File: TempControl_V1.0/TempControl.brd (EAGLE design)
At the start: 48.3 x 71.1 mm, 21 parts, among them J1 POWER_JACKPTH_BREAD, J3 10118194-0001LF, J4 6_PIN_SERIAL_CABLEPTH, U1 328P, Y1 16MHz

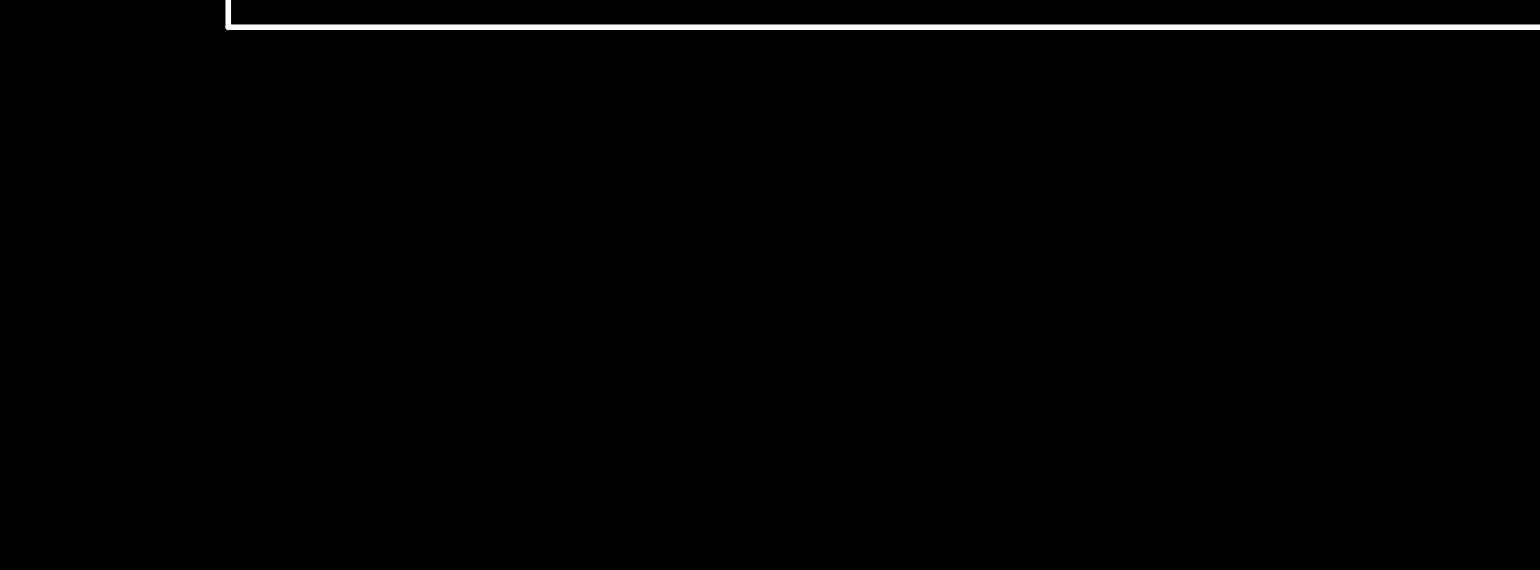
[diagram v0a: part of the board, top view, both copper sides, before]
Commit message: - Added .lbr file for TempControl project - Added OLED part - Rename the project name
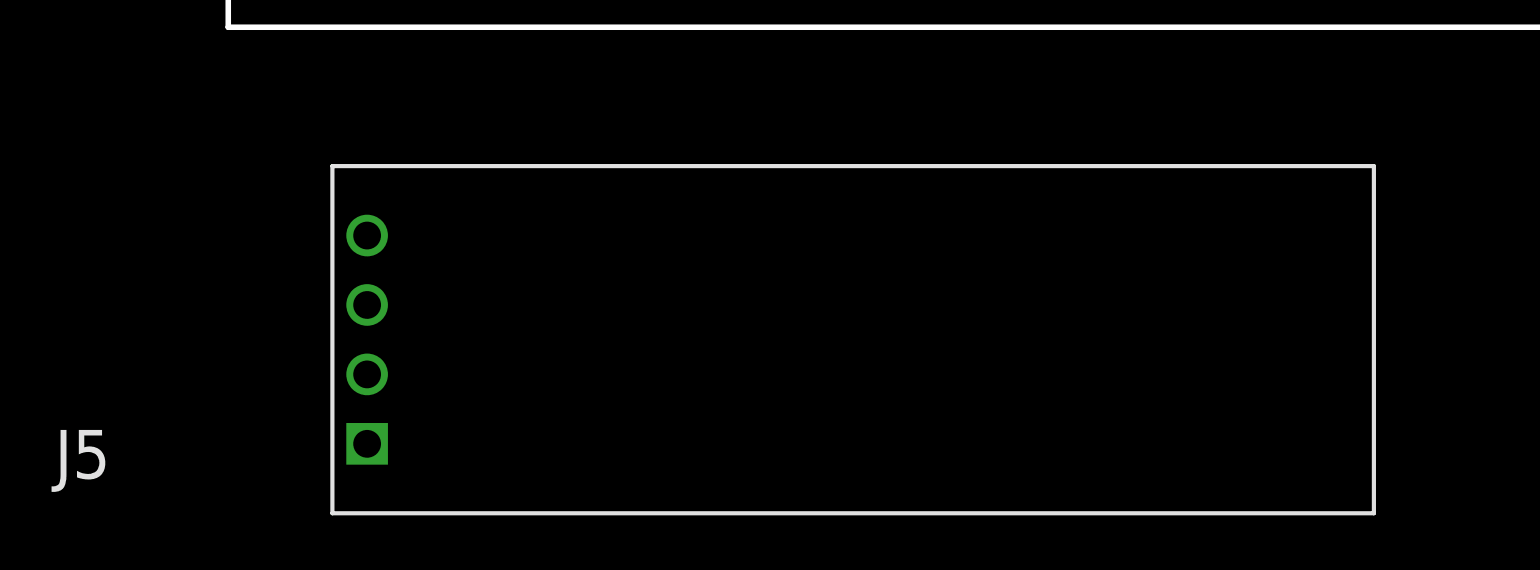
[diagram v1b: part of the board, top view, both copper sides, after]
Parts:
- added J5: OLED_128_32, BarnabasRobotics:OLED_128_32
- J1: value POWER_JACKPTH_BREAD -> SPARKFUN-CONNECTORS_POWER_JACKPTH_BREAD; device SparkFun-Connectors:POWER_JACK_PTH_BREAD -> BarnabasRobotics:SPARKFUN-CONNECTORS_POWER_JACK_PTH_BREAD
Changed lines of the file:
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@@
 <element name="D2" library="SparkFun-LED" package="LED_5MM" value="" x="36.83" y="22.86"/>
 <element name="D3" library="SparkFun-LED" package="LED_5MM" value="" x="36.83" y="11.43"/>
-<element name="J1" library="SparkFun-Connectors" package="POWER_JACK_PTH_BREAD" value="POWER_JACKPTH_BREAD" x="-2.54" y="64.77" rot="R270">
+<element name="J1" library="BarnabasRobotics" package="SPARKFUN-CONNECTORS_POWER_JACK_PTH_BREAD" value="SPARKFUN-CONNECTORS_POWER_JACKPTH_BREAD" x="-2.54" y="64.77" rot="R270">
 <attribute name="PROD_ID" value="PRT-10811" x="-2.54" y="64.77" size="1.778" layer="27" rot="R270" display="off"/>
 </element>
@@
 <attribute name="PROD_ID" value="CAP-08440" x="24.13" y="66.04" size="1.778" layer="27" rot="R180" display="off"/>
 </element>
+<element name="J5" library="BarnabasRobotics" package="OLED_128_32" value="OLED_128_32" x="5.08" y="-15.24"/>
 </elements>
 <signals>
